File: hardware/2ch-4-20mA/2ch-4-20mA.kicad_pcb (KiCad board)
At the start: 2 copper layers, 46.4 x 46.4 mm, 30 parts, among them J1 Conn_01x02, J2 Conn_01x02, J3 Conn_01x07, U1 LMP8640, U2 LMP8640, U3 TEC2-0913

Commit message: Updated PCB with new OSHW logo
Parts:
- G1: footprint BrechtVanEeckhoudt_Aesthetics:OSHW-EEVBLOG2_SPFMDBC_SolderMaskTop_5mm -> BrechtVE_Aesthetics:OSHW-Logo_5.7x6mm_SolderMask
- H1, H2, H3, H4: value MountingHole -> M3
- J1, J2: footprint PhoenixContact:PTSA 1,5 (1,5mm wire, 2 contacts, 3,5mm spacing) -> Connector_Phoenix_PTSA_extra:PhoenixContact_PTSA_1,5_2-G-3,5_1x02_P3.50mm_Angled

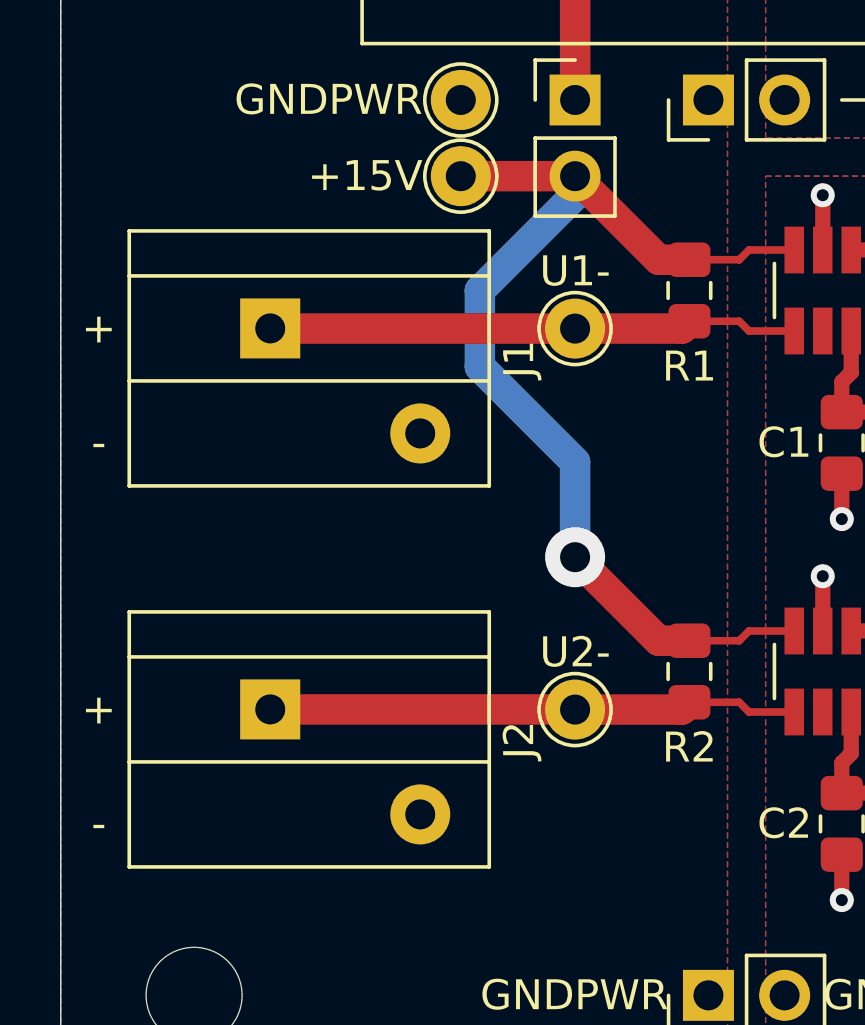
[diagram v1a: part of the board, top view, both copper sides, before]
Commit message: Updated header footprint
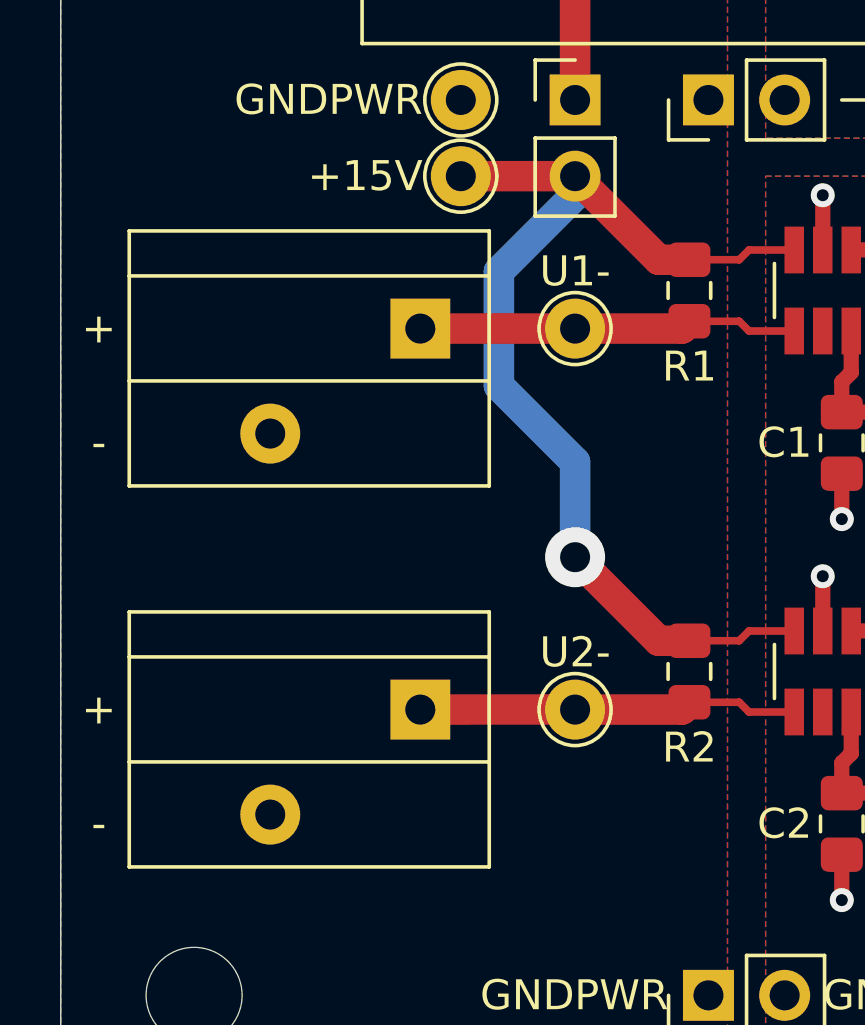
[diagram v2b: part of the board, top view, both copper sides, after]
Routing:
- net /M1-: track 18.1 -> 13.0 mm
- net /M2-: track 17.7 -> 12.7 mm
- net +15V: track 36.3 -> 35.8 mm
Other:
- board text added: "12/2019"
- board text added: "2 CH 4-20 mA to voltage v1.1"
- board text removed: "11/2019"
- board text removed: "2 CH 4-20 mA to voltage v1.0"
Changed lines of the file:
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@@
     (thickness 1.6)
     (drawings 50)
-    (tracks 88)
+    (tracks 87)
     (zones 0)
     (modules 30)
@@
     (add_net GNDPWR)
     (add_net "Net-(JP4-Pad1)")
-    (add_net "Net-(U3-Pad5)")
-    (add_net "Net-(U3-Pad8)")
     (add_net VDD)
     (add_net VDDA)
@@
     (descr "Generic Phoenix Contact connector footprint for: PTSA_1,5/_2-3,5; number of pins: 02; pin pitch: 3.50mm; Angled || order number: PTSA15235ZBK (2A 250V Black)")
     (tags "phoenix_contact connector PTSA_01x02_G_3.50mm")
-    (fp_text reference J2 (at 1.016 -8.2982 90) (layer F.SilkS)
+    (fp_text reference J2 (at 1.016 -8.2982 90) (layer F.SilkS) hide
       (effects (font (size 1 1) (thickness 0.15)))
     )
@@
     (fp_line (start 5.2446 4.7018) (end -3.2554 4.7018) (layer F.CrtYd) (width 0.12))
     (fp_line (start -3.2554 4.7018) (end -3.2554 -7.2982) (layer F.CrtYd) (width 0.12))
-    (pad 1 thru_hole rect (at -0.0054 0.0018 270) (size 2 2) (drill 1) (layers *.Cu *.Mask)
+    (pad 2 thru_hole circle (at 3.5 0.0018 270) (size 2 2) (drill 1) (layers *.Cu *.Mask)
+      (net 3 GNDPWR))
+    (pad 1 thru_hole rect (at 0 -5 270) (size 2 2) (drill 1) (layers *.Cu *.Mask)
       (net 5 /M2-))
-    (pad 2 thru_hole circle (at 3.4946 -4.9982 270) (size 2 2) (drill 1) (layers *.Cu *.Mask)
-      (net 3 GNDPWR))
   )
   (module Connector_Phoenix_PTSA_extra:PhoenixContact_PTSA_1,5_2-G-3,5_1x02_P3.50mm_Angled (layer F.Cu)
@@
     (descr "Generic Phoenix Contact connector footprint for: PTSA_1,5/_2-3,5; number of pins: 02; pin pitch: 3.50mm; Angled || order number: PTSA15235ZBK (2A 250V Black)")
     (tags "phoenix_contact connector PTSA_01x02_G_3.50mm")
-    (fp_text reference J1 (at 1.016 -8.2982 90) (layer F.SilkS)
+    (fp_text reference J1 (at 1.016 -8.2982 90) (layer F.SilkS) hide
       (effects (font (size 1 1) (thickness 0.15)))
     )
@@
     (fp_line (start 5.2446 4.7018) (end -3.2554 4.7018) (layer F.CrtYd) (width 0.12))
     (fp_line (start -3.2554 4.7018) (end -3.2554 -7.2982) (layer F.CrtYd) (width 0.12))
-    (pad 1 thru_hole rect (at -0.0054 0.0018 270) (size 2 2) (drill 1) (layers *.Cu *.Mask)
+    (pad 2 thru_hole circle (at 3.5 0.0018 270) (size 2 2) (drill 1) (layers *.Cu *.Mask)
+      (net 3 GNDPWR))
+    (pad 1 thru_hole rect (at 0 -5 270) (size 2 2) (drill 1) (layers *.Cu *.Mask)
       (net 4 /M1-))
-    (pad 2 thru_hole circle (at 3.4946 -4.9982 270) (size 2 2) (drill 1) (layers *.Cu *.Mask)
-      (net 3 GNDPWR))
   )
   (module BrechtVE_Aesthetics:OSHW-Logo_5.7x6mm_SolderMask (layer F.Cu)
@@
   )
   (gr_line (start 161.29 117.475) (end 135.89 117.475) (layer B.SilkS) (width 0.12))
-  (gr_text 11/2019 (at 136.525 116.205) (layer B.SilkS)
+  (gr_text 12/2019 (at 136.525 116.205) (layer B.SilkS)
     (effects (font (size 1 1) (thickness 0.15)) (justify right mirror))
   )
@@
     (effects (font (size 1 1) (thickness 0.15)) (justify left mirror))
   )
-  (gr_text "2 CH 4-20 mA to voltage v1.0" (at 160.655 112.395) (layer B.SilkS)
+  (gr_text "2 CH 4-20 mA to voltage v1.1" (at 160.655 112.395) (layer B.SilkS)
     (effects (font (size 1 1) (thickness 0.15)) (justify left mirror))
   )
@@
   (segment (start 143.51 113.665) (end 143.51 100.965) (width 0.508) (layer B.Cu) (net 2))
   (segment (start 132.96 98.18) (end 132.715 98.425) (width 1.016) (layer F.Cu) (net 4))
-  (segment (start 122.5586 98.425) (end 122.5532 98.4196) (width 1.016) (layer F.Cu) (net 4))
-  (segment (start 132.715 98.425) (end 122.5586 98.425) (width 1.016) (layer F.Cu) (net 4))
   (segment (start 136.28 98.425) (end 136.525 98.18) (width 1.016) (layer F.Cu) (net 4))
   (segment (start 132.715 98.425) (end 136.28 98.425) (width 1.016) (layer F.Cu) (net 4))
@@
   (segment (start 138.51 98.505) (end 140.02 98.505) (width 0.254) (layer F.Cu) (net 4))
   (segment (start 138.185 98.18) (end 138.51 98.505) (width 0.254) (layer F.Cu) (net 4))
-  (segment (start 132.7096 111.1196) (end 132.715 111.125) (width 1.016) (layer F.Cu) (net 5))
-  (segment (start 122.5532 111.1196) (end 132.7096 111.1196) (width 1.016) (layer F.Cu) (net 5))
+  (segment (start 132.715 98.425) (end 127.555 98.425) (width 1.016) (layer F.Cu) (net 4))
   (segment (start 136.28 111.125) (end 136.525 110.88) (width 1.016) (layer F.Cu) (net 5))
   (segment (start 132.715 111.125) (end 136.28 111.125) (width 1.016) (layer F.Cu) (net 5))
@@
   (segment (start 138.51 111.205) (end 140.02 111.205) (width 0.254) (layer F.Cu) (net 5))
   (segment (start 138.185 110.88) (end 138.51 111.205) (width 0.254) (layer F.Cu) (net 5))
+  (segment (start 132.7096 111.1196) (end 132.715 111.125) (width 1.016) (layer F.Cu) (net 5))
+  (segment (start 127.555 111.125) (end 132.7096 111.1196) (width 1.016) (layer F.Cu) (net 5))
   (segment (start 140.335 83.185) (end 140.335 85.725) (width 0.508) (layer F.Cu) (net 6))
   (segment (start 142.24 81.28) (end 140.335 83.185) (width 0.508) (layer F.Cu) (net 6))
@@
   (segment (start 132.715 93.345) (end 135.5 96.13) (width 1.016) (layer F.Cu) (net 11))
   (segment (start 128.905 93.345) (end 132.715 93.345) (width 1.016) (layer F.Cu) (net 11))
-  (segment (start 132.715 93.345) (end 132.715 93.98) (width 1.016) (layer B.Cu) (net 11))
-  (segment (start 132.715 93.98) (end 129.54 97.155) (width 1.016) (layer B.Cu) (net 11))
-  (segment (start 129.54 97.155) (end 129.54 99.695) (width 1.016) (layer B.Cu) (net 11))
-  (segment (start 132.715 102.87) (end 132.715 106.045) (width 1.016) (layer B.Cu) (net 11))
-  (segment (start 129.54 99.695) (end 132.715 102.87) (width 1.016) (layer B.Cu) (net 11))
   (segment (start 135.5 108.83) (end 136.525 108.83) (width 1.016) (layer F.Cu) (net 11))
   (segment (start 132.715 106.045) (end 135.5 108.83) (width 1.016) (layer F.Cu) (net 11))
+  (segment (start 132.715 102.87) (end 132.715 106.045) (width 1.016) (layer B.Cu) (net 11))
+  (segment (start 130.175 100.33) (end 132.715 102.87) (width 1.016) (layer B.Cu) (net 11))
+  (segment (start 130.175 96.52) (end 130.175 100.33) (width 1.016) (layer B.Cu) (net 11))
+  (segment (start 132.715 93.345) (end 132.715 93.98) (width 1.016) (layer B.Cu) (net 11))
+  (segment (start 132.715 93.98) (end 130.175 96.52) (width 1.016) (layer B.Cu) (net 11))
   (segment (start 132.715 85.725) (end 132.715 90.805) (width 1.016) (layer F.Cu) (net 12))
   (zone (net 3) (net_name GNDPWR) (layer B.Cu) (hatch edge 0.508)
